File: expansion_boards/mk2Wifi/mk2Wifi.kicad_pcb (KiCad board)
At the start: 2 copper layers, 51 x 26 mm, 22 parts, among them J4 OLED, SW1 GPIO0, SW2 RESET, U1 ESP32-WROOM-32E, U2 AP2112R5-3.3TRG1

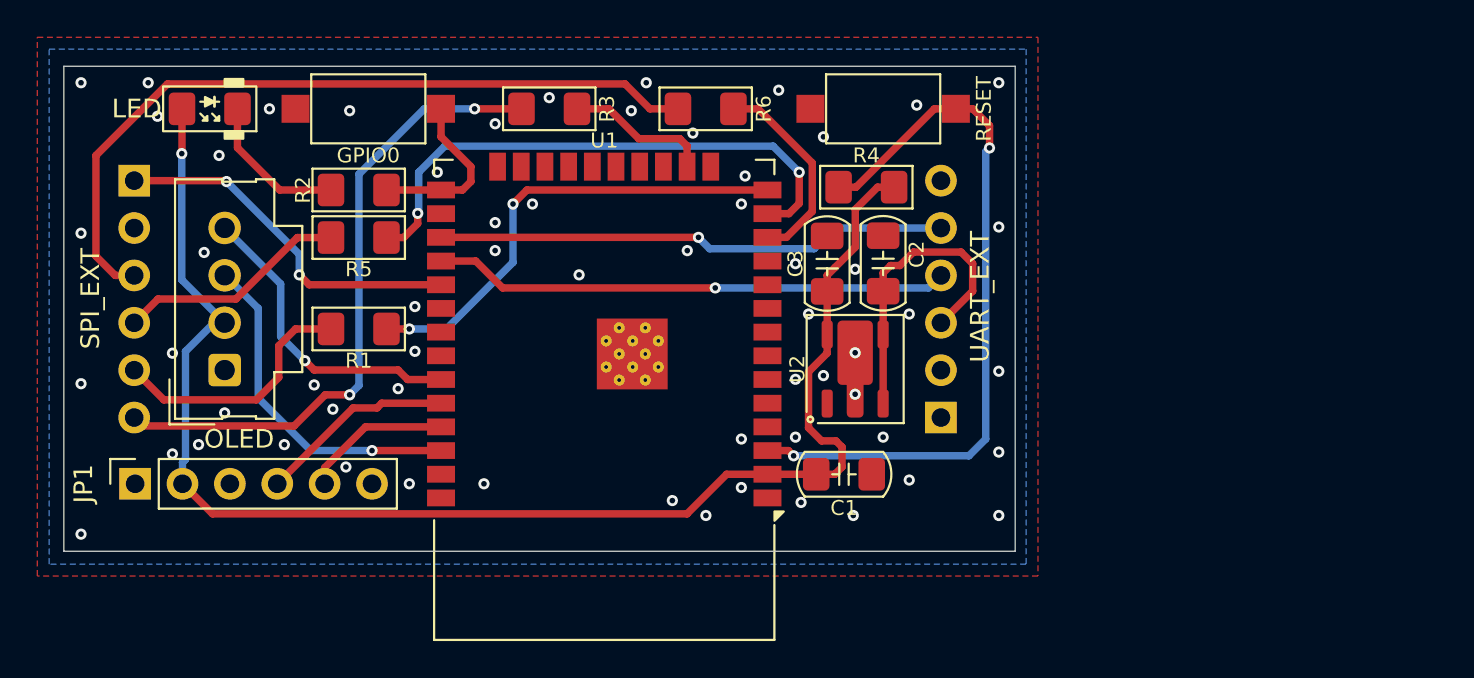
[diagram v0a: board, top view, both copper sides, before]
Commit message: Wire remaining ESP32-C3 GPIOs and fix mk2Wifi ERC errors
Connect GPIO3 (DS18B20), GPIO5 (SDA), GPIO6 (SCL) directly and
GPIO7 (D8) through R11 (1K) protection resistor. Fix duplicate
power symbol references (#PWR01/03/04/08), add UserDef symbol
library to sym-lib-table, and add PWR_FLAG symbols to +5V, +3.3V,
and GND nets to resolve all ERC errors.

Co-Authored-By: Claude Opus 4.6 <noreply@anthropic.com>
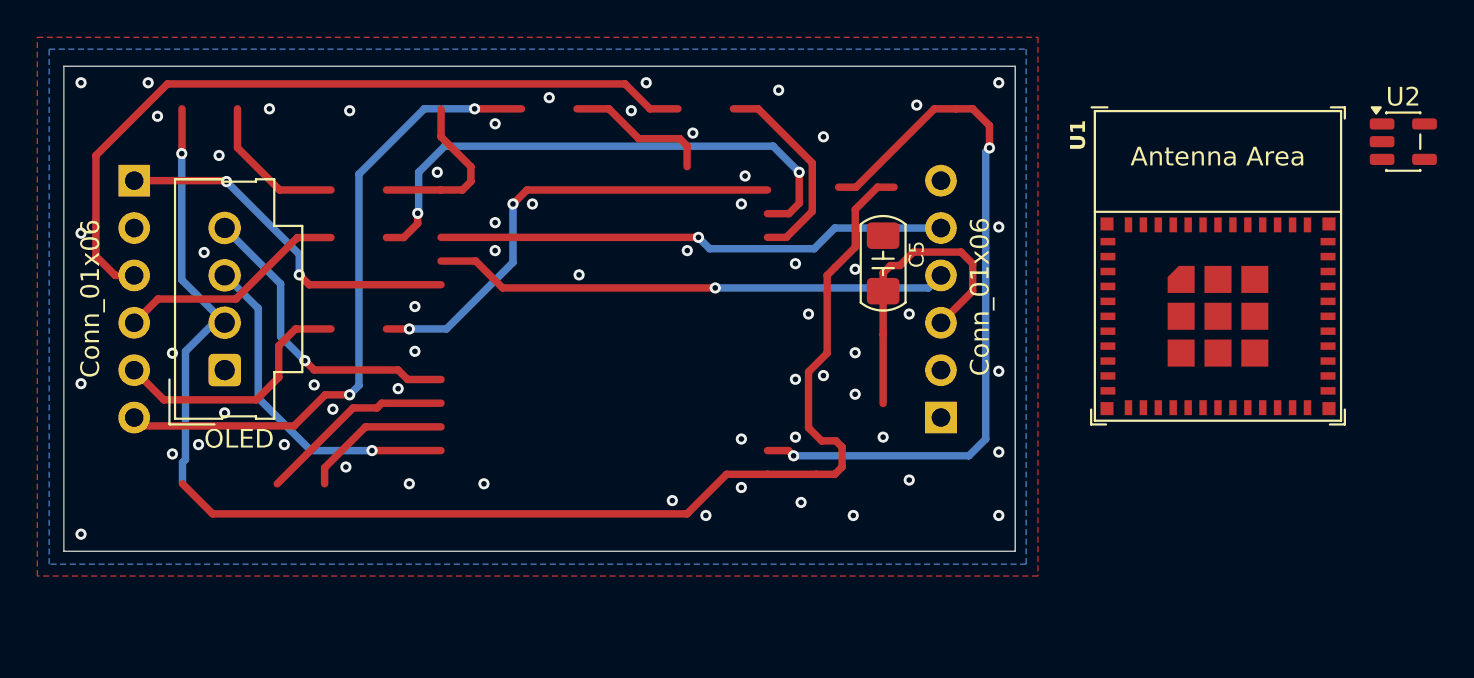
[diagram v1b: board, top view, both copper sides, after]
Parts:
- removed C1: 100nF, PCM_Capacitor_SMD_Handsoldering_AKL:C_1206_3216Metric_Pad1.42x1.75mm
- removed C3: 4u7, PCM_Capacitor_SMD_Handsoldering_AKL:C_1206_3216Metric_Pad1.42x1.75mm
- removed JP1: UART_ESP32, Connector_PinSocket_2.54mm:PinSocket_1x06_P2.54mm_Vertical
- removed LED1: LED, PCM_LED_SMD_Handsoldering_AKL:LED_1206_3216Metric_Pad1.42x1.75mm
- removed R1, R2, R3, R5, R6: 1K, PCM_Resistor_SMD_AKL:R_1206_3216Metric_Pad1.42x1.75mm_HandSolder
- removed R4: 10K, PCM_Resistor_SMD_AKL:R_1206_3216Metric_Pad1.42x1.75mm_HandSolder
- removed SW1: GPIO0, Button_Switch_SMD:SW_SPST_CK_RS282G05A3
- removed SW2: RESET, Button_Switch_SMD:SW_SPST_CK_RS282G05A3
- C5: renamed from C2; value 4u7 -> C
- J0: renamed from SPI_EXT0; value SPI_EXT -> Conn_01x06
- J3: renamed from JP3; value UART_EXT -> Conn_01x06
- U1: value ESP32-WROOM-32E -> ESP32-C3-MINI-1; footprint RF_Module:ESP32-WROOM-32D -> PCM_Espressif:ESP32-C3-MINI-1
- U2: value AP2112R5-3.3TRG1 -> AP2112K-3.3; footprint PCM_Package_TO_SOT_SMD_AKL:Diodes_SOT-89-5 -> Package_TO_SOT_SMD:SOT-23-5
- moved U1 33.2 mm to (112.5, 50.9), turned to 0 degrees
- moved U2 31.8 mm to (122.4, 44.3), turned to 0 degrees
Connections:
- J0 pad 1: /DS18B20 -> GND
- J0 pad 2: GND -> /D8
- J0 pad 3: /RFM_SEL/D10 -> /D7
- J0 pad 4: /RFM_SCK/D13 -> /D6
- J0 pad 5: /RFM_MISO/D12 -> /D5
- J0 pad 6: /RFM_MOSI/D11 -> /D9
- J3 pad 2: unconnected-(JP3-Pin_2-Pad2) -> /DS18B20
- J3 pad 4: /AVR_RX -> /UART_RX
- J3 pad 5: /AVR_TX -> /UART_TX
- J4 pad 2: +3V3 -> +3.3V
- U1 pad 11: unconnected-(U1-IO26-Pad11) -> GND
- U1 pad 14: Net-(U1-IO12) -> GND
- U1 pad 15: GND -> unconnected-(U1-NC-Pad15)
- U1 pad 18: unconnected-(U1-NC-Pad18) -> Net-(U1-GPIO4/ADC1_CH4)
- U1 pad 19: unconnected-(U1-NC-Pad19) -> /SDA
- U1 pad 2: +3V3 -> GND
- U1 pad 20: unconnected-(U1-NC-Pad20) -> /SCL
- U1 pad 21: unconnected-(U1-NC-Pad21) -> Net-(U1-GPIO7)
- U1 pad 22: unconnected-(U1-NC-Pad22) -> /GPIO8
- U1 pad 23: unconnected-(U1-IO15-Pad23) -> /GPIO9
- U1 pad 25: /GPIO0 -> unconnected-(U1-NC-Pad25)
- U1 pad 26: unconnected-(U1-IO4-Pad26) -> /USB_DN
- U1 pad 27: /AVR_TX -> /USB_DP
- U1 pad 28: /AVR_RX -> unconnected-(U1-NC-Pad28)
- U1 pad 29: /DS18B20 -> unconnected-(U1-NC-Pad29)
- U1 pad 3: /RESET -> +3V3
- U1 pad 30: unconnected-(U1-IO18-Pad30) -> /UART_RX
- U1 pad 31: unconnected-(U1-IO19-Pad31) -> /UART_TX
- U1 pad 33: /SDA -> unconnected-(U1-NC-Pad33)
- U1 pad 34: /ESP_RX -> unconnected-(U1-NC-Pad34)
- U1 pad 35: /ESP_TX -> unconnected-(U1-NC-Pad35)
- U1 pad 36: /SCL -> GND
- U1 pad 37: unconnected-(U1-IO23-Pad37) -> GND
- U1 pad 5: unconnected-(U1-SENSOR_VN-Pad5) -> /GPIO2
- U1 pad 6: unconnected-(U1-IO34-Pad6) -> /DS18B20
- U1 pad 8: unconnected-(U1-IO32-Pad8) -> Net-(U1-EN/CHIP_PU)
- U2 pad 1: unconnected-(U2-NC-Pad1) -> +5V
- U2 pad 4: +5V -> unconnected-(U2-NC-Pad4)
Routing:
- net (no net): track 0.00 -> 149.3 mm, vias 0 -> 6
- net /RFM_SEL/D10: track 41.2 -> 0.00 mm
- net /D7: track 0.00 -> 41.2 mm
- net /RESET: track 39.3 -> 0.00 mm, vias 2 -> 0
- net /RFM_MOSI/D11: track 34.6 -> 0.00 mm, vias 2 -> 0
- net /D9: track 0.00 -> 34.6 mm, vias 0 -> 2
- net Net-(U1-GPIO1/ADC1_CH1/XTAL_32K_N): track 29.9 -> 0.00 mm, vias 2 -> 0
- net /UART_RX: track 0.00 -> 27.7 mm, vias 0 -> 1
- net /AVR_RX: track 27.7 -> 0.00 mm, vias 1 -> 0
- net /UART_TX: track 0.00 -> 27.5 mm, vias 0 -> 1
- net /AVR_TX: track 27.5 -> 0.00 mm, vias 1 -> 0
- net Net-(U1-IO12): track 25.3 -> 0.00 mm, vias 2 -> 0
- net +3V3: track 78.0 -> 55.7 mm, vias 1 -> 0
- net +3.3V: track 0.00 -> 22.3 mm, vias 0 -> 1
- net GND: track 0.00 -> 19.4 mm, vias 61 -> 63
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
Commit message: Finalize mk2Wifi PCB layout, project settings, and 3D model
Update PCB layout with component placement and routing for all
newly footprinted parts. Adjust zone clearance (0.25mm) and via
sizes (0.8/0.4mm) in project settings. Add UserDef footprint
library to fp-lib-table. Include ESP32-C3-MINI-1 STEP 3D model.

Co-Authored-By: Claude Opus 4.6 <noreply@anthropic.com>
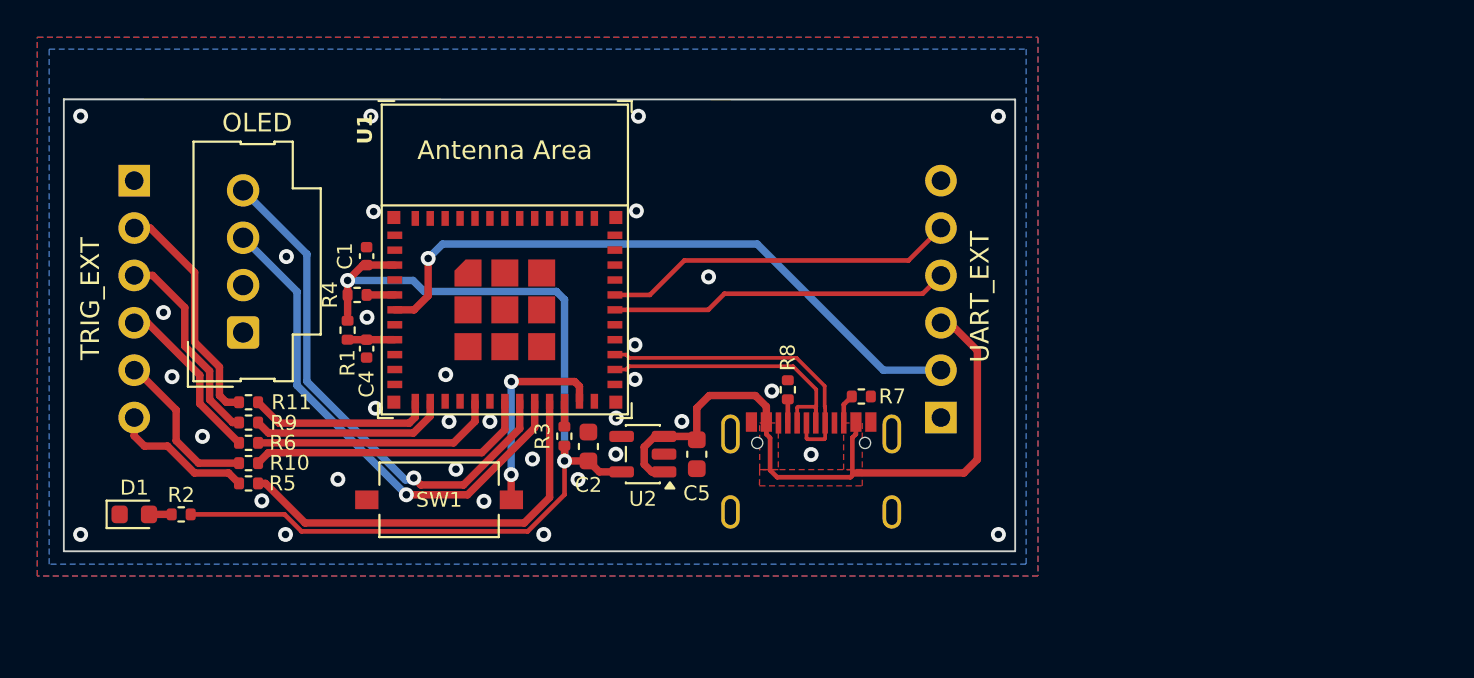
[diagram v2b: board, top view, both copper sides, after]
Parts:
- removed kibuzzard-64EB6544-2: G010, kibuzzard-64EB6544-2
- removed kibuzzard-68375C5E: G***, kibuzzard-68375C5E
- added C1: 100n, Capacitor_SMD:C_0402_1005Metric, F.Cu at (66.8, 50.4)
- added C2: 4u7, Capacitor_SMD:C_0603_1608Metric, F.Cu at (78.7, 60.6)
- added C4: 100n, Capacitor_SMD:C_0402_1005Metric, F.Cu at (66.8, 55.4)
- added D1: LED, LED_SMD:LED_0603_1608Metric, F.Cu at (54.4, 64.2)
- added J2: USB_C_Receptacle_USB2.0_16P, valcon-usb:CSP-USC16-TR, F.Cu at (90.9, 62.8)
- added R1: 10K, Resistor_SMD:R_0402_1005Metric, F.Cu at (65.8, 54.4)
- added R10: 1K, Resistor_SMD:R_0402_1005Metric, F.Cu at (60.5, 61.5)
- added R11: 1K, Resistor_SMD:R_0402_1005Metric, F.Cu at (60.5, 58.2)
- added R2: 1K, Resistor_SMD:R_0402_1005Metric, F.Cu at (56.9, 64.2)
- added R3: 10K, Resistor_SMD:R_0402_1005Metric, F.Cu at (77.4, 60.1)
- added R4: 10K, Resistor_SMD:R_0402_1005Metric, F.Cu at (66.3, 52.5)
- added R5: 1K, Resistor_SMD:R_0402_1005Metric, F.Cu at (60.5, 62.6)
- added R6: 1K, Resistor_SMD:R_0402_1005Metric, F.Cu at (60.5, 60.4)
- added R7: 5K1, Resistor_SMD:R_0402_1005Metric, F.Cu at (93.3, 57.9)
- added R8: 5K1, Resistor_SMD:R_0402_1005Metric, F.Cu at (89.4, 57.6)
- added R9: 1K, Resistor_SMD:R_0402_1005Metric, F.Cu at (60.5, 59.3)
- added SW1: SW_Push, Button_Switch_SMD:SW_Tactile_SPST_NO_Straight_CK_PTS636Sx25SMTRLFS, F.Cu at (70.7, 63.5)
- added kibuzzard-69922598: G***, kibuzzard-69922598, B.Cu at (76.1, 43.7)
- added kibuzzard-699225A4: G***, kibuzzard-699225A4, B.Cu at (76.1, 47.3)
- C5: value C -> 4u7; footprint PCM_Capacitor_SMD_Handsoldering_AKL:C_1206_3216Metric_Pad1.42x1.75mm -> Capacitor_SMD:C_0603_1608Metric
- J0: value Conn_01x06 -> TRIG_EXT
- J3: value Conn_01x06 -> UART_EXT
- moved U2 44.1 mm to (81.6, 61.0), turned to 180 degrees
- moved U1 38.2 mm to (74.2, 50.6)
- moved C5 14.3 mm to (84.5, 61.0), turned to -90 degrees
- moved J4 2.25 mm to (60.2, 54.5)
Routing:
- net (no net): track 149.3 -> 0.00 mm, vias 6 -> 0
- net /DS18B20: track 0.00 -> 34.7 mm, vias 0 -> 1
- net /D7: track 41.2 -> 11.0 mm
- net /D9: track 34.6 -> 7.66 mm, vias 2 -> 0
- net +3.3V: track 22.3 -> 0.00 mm, vias 1 -> 0
- net Net-(U1-GPIO7): track 0.00 -> 22.2 mm
- net +5V: track 16.4 -> 37.5 mm
- net GND: track 19.4 -> 0.00 mm, vias 63 -> 33
- net /USB_DP: track 0.00 -> 16.6 mm
- net /USB_DN: track 0.00 -> 15.9 mm
- net Net-(U1-GPIO4/ADC1_CH4): track 0.00 -> 15.5 mm
- net Net-(U1-GPIO10): track 0.00 -> 13.2 mm
- net /D8: track 0.00 -> 12.6 mm
- net /SDA: track 16.6 -> 28.2 mm
- net /GPIO9: track 0.00 -> 10.9 mm, vias 0 -> 2
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- added copper zone on F.Cu, net +5V
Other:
- board size 51 x 26 mm -> 51 x 24.2 mm
- board text added: "mk2Wifi ESP32 Expansion Board"
- board text removed: "Mk2PVRouter ESP32 Expansion Board"

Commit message: Add mk2Wifi documentation, board images, and PCB/schematic updates
Add bilingual README (French default, English translation) with BOM,
connector pinouts, GPIO mapping, power supply details, programming
instructions, and USB-C safety warning. Include trimmed 3D render
images (front, back, SMD, bare board) in assets/ folder.

Co-Authored-By: Claude Opus 4.6 <noreply@anthropic.com>
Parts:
- removed kibuzzard-699225A4: G***, kibuzzard-699225A4
- added G***: LOGO, LOGO, F.Cu at (89.1, 49.1)
- added kibuzzard-69931B12: G***, kibuzzard-69931B12, B.Cu at (76.1, 47.3)
- moved R2 2.76 mm to (54.1, 63.9), turned to 90 degrees
- moved D1 1.59 mm to (52.8, 64.2), turned to 90 degrees
- moved J0 0.41 mm to (54.4, 45.9)
- moved J3 0.41 mm to (97.6, 58.6)
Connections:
- U1 pad 30: /UART_RX -> /UART_TX
- U1 pad 31: /UART_TX -> /UART_RX
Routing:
- net +3V3: track 52.5 -> 55.7 mm
- net /D5: track 8.65 -> 9.26 mm
- net +5V: track 37.5 -> 38.1 mm
- net /D8: track 12.6 -> 13.1 mm
- net /UART_TX: track 19.0 -> 19.5 mm, vias 0 -> 1
- net GND: vias 33 -> 42
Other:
- board text added: "mk2WiFi v1.0"
- board text removed: "mk2Wifi ESP32 Expansion Board"

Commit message: Add solder jumpers to mk2Wifi and custom smaller solder jumper footprint
New UserDef footprint: SolderJumper-2_P1.0mm_Open_Pad0.8x1.2mm (compact
1.0mm pitch, 0.8x1.2mm pads, 0.2mm gap for hand soldering).

Co-Authored-By: Claude Opus 4.6 <noreply@anthropic.com>
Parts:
- added JP1: D8, UserDef:SolderJumper-2_P1.0mm_Open_Pad0.8x1.2mm, F.Cu at (61.5, 58.3)
- added JP2: D7, UserDef:SolderJumper-2_P1.0mm_Open_Pad0.8x1.2mm, F.Cu at (59.1, 59.4)
- added JP3: D6, UserDef:SolderJumper-2_P1.0mm_Open_Pad0.8x1.2mm, F.Cu at (61.5, 60.5)
- added JP4: D5, UserDef:SolderJumper-2_P1.0mm_Open_Pad0.8x1.2mm, F.Cu at (59.1, 61.6)
- added JP5: D9, UserDef:SolderJumper-2_P1.0mm_Open_Pad0.8x1.2mm, F.Cu at (61.5, 62.7)
- moved R5 3.14 mm to (63.6, 61.6)
- moved R6 3.14 mm to (63.6, 60.5)
- moved R7 3.14 mm to (63.6, 59.4)
- moved R8 3.14 mm to (63.6, 58.3)
- moved R9 3.14 mm to (63.6, 62.6)
- moved J4 0.31 mm to (60.0, 54.2)
- renumbered R8 to R10, R7 to R11, R10 to R5, R9 to R7, R11 to R8, R5 to R9
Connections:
- J0 pad 2: /D8 -> Net-(J0-Pin_2)
- J0 pad 3: /D7 -> Net-(J0-Pin_3)
- J0 pad 4: /D6 -> Net-(J0-Pin_4)
- J0 pad 5: /D5 -> Net-(J0-Pin_5)
- J0 pad 6: /D9 -> Net-(J0-Pin_6)
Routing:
- net Net-(J0-Pin_2): track 0.00 -> 14.0 mm
- net Net-(J0-Pin_4): track 0.00 -> 12.2 mm
- net /D8: track 13.1 -> 1.10 mm
- net Net-(J0-Pin_3): track 0.00 -> 11.2 mm
- net Net-(J0-Pin_6): track 0.00 -> 8.46 mm
- net Net-(J0-Pin_5): track 0.00 -> 8.24 mm
- net /D6: track 9.34 -> 1.10 mm
- net /D7: track 11.2 -> 3.47 mm
- net /D9: track 8.08 -> 1.10 mm
- net /D5: track 9.26 -> 3.47 mm
- net Net-(U1-GPIO7): track 22.2 -> 19.0 mm
- net Net-(U1-GPIO0/ADC1_CH0/XTAL_32K_P): track 9.88 -> 6.71 mm
- net Net-(U1-GPIO1/ADC1_CH1/XTAL_32K_N): track 10.6 -> 7.47 mm
- net Net-(U1-GPIO10): track 13.2 -> 10.1 mm
- net Net-(U1-GPIO4/ADC1_CH4): track 15.5 -> 12.4 mm
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
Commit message: Fix split 3.3V power net on mk2Wifi OLED connector
J4 (OLED) VCC pin was on +3.3V (net 13) while the rest of the board
uses +3V3 (net 6), creating two separate unconnected power nets.
Changed #PWR6 to +3V3 in schematic and reassigned J4 pad 2 in PCB.

Co-Authored-By: Claude Opus 4.6 <noreply@anthropic.com>
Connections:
- J4 pad 2: +3.3V -> +3V3
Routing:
- net +3V3: track 55.7 -> 61.5 mm
- net GND: vias 45 -> 48
